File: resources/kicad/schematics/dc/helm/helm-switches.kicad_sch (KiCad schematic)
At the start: 46 parts, among them SW01 CARLING_BLANK, SW02 CARLING_TYPE_28_(ON)-OFF-(ON), SW03 CARLING_TYPE_22_OFF-(ON), SW04 CARLING_TYPE_62_OFF-ON-ON, SW05 CARLING_TYPE_21_OFF-ON, SW06 CARLING_BLANK, SW07 CARLING_BLANK, SW08 CARLING_BLANK, SW09 CARLING_TYPE_21_OFF-ON, SW10 CARLING_TYPE_21_OFF-ON, SW11 CARLING_TYPE_21_OFF-ON, SW12 CARLING_TYPE_21_OFF-ON, SW13 CARLING_TYPE_21_OFF-ON, SW14 CARLING_TYPE_21_OFF-ON, SW15 CARLING_TYPE_21_OFF-ON, SW16 CARLING_TYPE_62_OFF-ON-ON, SW17 CARLING_TYPE_24_ON-ON, SW18 CARLING_TYPE_22_OFF-(ON), SW19 CARLING_TYPE_62_OFF-ON-ON, SW20 CARLING_TYPE_62_OFF-ON-ON, SW21 CARLING_TYPE_62_OFF-ON-ON, SW22 CARLING_TYPE_62_OFF-ON-ON, SW23 CARLING_BLANK, SW24 CARLING_TYPE_62_OFF-ON-ON, SW25 CARLING_TYPE_21_OFF-ON, SW26 CARLING_V_SERIES_ROTARY_TYPE_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, SW27 CARLING_TYPE_62_OFF-ON-ON, SW28 CARLING_TYPE_28_(ON)-OFF-(ON), SW29 CARLING_TYPE_28_(ON)-OFF-(ON), SW30 CARLING_TYPE_28_(ON)-OFF-(ON), SW31 CARLING_TYPE_62_OFF-ON-ON, SW32 CARLING_TYPE_62_OFF-ON-ON, SW33 CARLING_BLANK, SW34 CARLING_BLANK, SW35 CARLING_BLANK, SW36 CARLING_TYPE_62_OFF-ON-ON, SW37 CARLING_TYPE_21_OFF-ON, SW38 CARLING_TYPE_21_OFF-ON, SW39 CARLING_TYPE_26_ON-OFF-ON

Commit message: Updates
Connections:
- net F9.2.1: now also SW37.12 (LED+); no longer SW26.8 (LED+), SW27.10 (LED+), SW27.12 (LED+), SW28.10 (LED+), SW28.2, SW29.10 (LED+), SW29.2, SW30.10 (LED+), SW30.2
- net F9.2.8: no longer SW27.3
- net ENG.IGN renamed IGN.75
- net ENG.IGN.TRL.SBY renamed IGN.75.TRL.SBY
- net IGN.75.TRL.SBY: no longer SW37.12 (LED+)
- net F9.2.1.DKH.OP1: no longer names the net of SW25.12 (LED+), SW25.4
- net F9.2.1.DKH.OP1: now also SW26.8 (LED+), SW27.10 (LED+), SW27.12 (LED+), SW28.10 (LED+), SW28.2, SW29.10 (LED+), SW29.2, SW30.10 (LED+), SW30.2
- new net F9.2.8.THR.ACT: SW27.3
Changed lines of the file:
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@@
 	)
 	(junction
-		(at 67.31 288.29)
-		(diameter 0)
-		(color 0 0 0 0)
-	)
-	(junction
-		(at 67.31 407.67)
-		(diameter 0)
-		(color 0 0 0 0)
-	)
-	(junction
 		(at 334.01 97.79)
 		(diameter 0)
@@
 	)
 	(junction
-		(at 67.31 389.89)
-		(diameter 0)
-		(color 0 0 0 0)
-	)
-	(junction
 		(at 120.65 389.89)
 		(diameter 0)
@@
 	)
 	(junction
+		(at 69.85 397.51)
+		(diameter 0)
+		(color 0 0 0 0)
+	)
+	(junction
 		(at 41.91 397.51)
 		(diameter 0)
@@
 	)
 	(junction
+		(at 95.25 288.29)
+		(diameter 0)
+		(color 0 0 0 0)
+	)
+	(junction
 		(at 227.33 233.68)
 		(diameter 0)
@@
 	)
 	(junction
-		(at 67.31 306.07)
-		(diameter 0)
-		(color 0 0 0 0)
-	)
-	(junction
 		(at 41.91 124.46)
 		(diameter 0)
@@
 	)
 	(junction
+		(at 69.85 389.89)
+		(diameter 0)
+		(color 0 0 0 0)
+	)
+	(junction
 		(at 92.71 226.06)
 		(diameter 0)
@@
 	)
 	(junction
+		(at 69.85 306.07)
+		(diameter 0)
+		(color 0 0 0 0)
+	)
+	(junction
 		(at 41.91 194.31)
 		(diameter 0)
@@
 	)
 	(junction
-		(at 95.25 288.29)
-		(diameter 0)
-		(color 0 0 0 0)
-	)
-	(junction
 		(at 95.25 331.47)
 		(diameter 0)
@@
 	(wire
 		(pts
-			(xy 67.31 389.89) (xy 67.31 397.51)
-		)
-		(stroke
-			(width 0)
-			(type default)
-		)
-	)
-	(wire
-		(pts
 			(xy 171.45 194.31) (xy 173.99 194.31)
 		)
@@
 	(wire
 		(pts
-			(xy 64.77 407.67) (xy 67.31 407.67)
-		)
-		(stroke
-			(width 0)
-			(type default)
-		)
-	)
-	(wire
-		(pts
 			(xy 120.65 31.75) (xy 173.99 31.75)
 		)
@@
 	(wire
 		(pts
-			(xy 69.85 290.83) (xy 69.85 306.07)
+			(xy 69.85 288.29) (xy 69.85 306.07)
 		)
 		(stroke
@@
 	(wire
 		(pts
-			(xy 69.85 306.07) (xy 67.31 306.07)
-		)
-		(stroke
-			(width 0)
-			(type default)
-		)
-	)
-	(wire
-		(pts
 			(xy 173.99 252.73) (xy 173.99 257.81)
 		)
@@
 	(wire
 		(pts
+			(xy 69.85 389.89) (xy 69.85 397.51)
+		)
+		(stroke
+			(width 0)
+			(type default)
+		)
+	)
+	(wire
+		(pts
 			(xy 308.61 257.81) (xy 308.61 252.73)
 		)
@@
 	(wire
 		(pts
-			(xy 31.75 389.89) (xy 67.31 389.89)
+			(xy 31.75 389.89) (xy 69.85 389.89)
 		)
 		(stroke
@@
 	(wire
 		(pts
-			(xy 64.77 410.21) (xy 67.31 410.21)
+			(xy 64.77 410.21) (xy 69.85 410.21)
 		)
 		(stroke
@@
 	(wire
 		(pts
-			(xy 64.77 397.51) (xy 67.31 397.51)
-		)
-		(stroke
-			(width 0)
-			(type default)
-		)
-	)
-	(wire
-		(pts
 			(xy 227.33 128.27) (xy 280.67 128.27)
 		)
@@
 	(wire
 		(pts
-			(xy 71.12 290.83) (xy 69.85 290.83)
-		)
-		(stroke
-			(width 0)
-			(type default)
-		)
-	)
-	(wire
-		(pts
 			(xy 171.45 41.91) (xy 173.99 41.91)
 		)
@@
 	(wire
 		(pts
+			(xy 64.77 402.59) (xy 72.39 402.59)
+		)
+		(stroke
+			(width 0)
+			(type default)
+		)
+	)
+	(wire
+		(pts
 			(xy 95.25 92.71) (xy 95.25 97.79)
 		)
@@
 	(wire
 		(pts
-			(xy 67.31 407.67) (xy 69.85 407.67)
+			(xy 64.77 407.67) (xy 72.39 407.67)
 		)
 		(stroke
@@
 	(wire
 		(pts
-			(xy 67.31 389.89) (xy 120.65 389.89)
-		)
-		(stroke
-			(width 0)
-			(type default)
-		)
-	)
-	(wire
-		(pts
 			(xy 97.79 194.31) (xy 95.25 194.31)
 		)
@@
 	(wire
 		(pts
+			(xy 69.85 397.51) (xy 69.85 410.21)
+		)
+		(stroke
+			(width 0)
+			(type default)
+		)
+	)
+	(wire
+		(pts
 			(xy 120.65 196.85) (xy 120.65 214.63)
 		)
@@
 	(wire
 		(pts
+			(xy 95.25 288.29) (xy 69.85 288.29)
+		)
+		(stroke
+			(width 0)
+			(type default)
+		)
+	)
+	(wire
+		(pts
 			(xy 64.77 351.79) (xy 69.85 351.79)
 		)
@@
 	(wire
 		(pts
-			(xy 64.77 306.07) (xy 67.31 306.07)
+			(xy 64.77 306.07) (xy 69.85 306.07)
 		)
 		(stroke
@@
 	(wire
 		(pts
-			(xy 67.31 410.21) (xy 67.31 407.67)
-		)
-		(stroke
-			(width 0)
-			(type default)
-		)
-	)
-	(wire
-		(pts
 			(xy 201.93 448.31) (xy 201.93 461.01)
 		)
@@
 	(wire
 		(pts
-			(xy 64.77 308.61) (xy 67.31 308.61)
+			(xy 64.77 308.61) (xy 69.85 308.61)
 		)
 		(stroke
@@
 	(wire
 		(pts
-			(xy 67.31 288.29) (xy 95.25 288.29)
-		)
-		(stroke
-			(width 0)
-			(type default)
-		)
-	)
-	(wire
-		(pts
 			(xy 95.25 306.07) (xy 95.25 311.15)
 		)
@@
 	(wire
 		(pts
-			(xy 64.77 402.59) (xy 69.85 402.59)
-		)
-		(stroke
-			(width 0)
-			(type default)
-		)
-	)
-	(wire
-		(pts
 			(xy 97.79 105.41) (xy 95.25 105.41)
 		)
@@
 	(wire
 		(pts
-			(xy 67.31 306.07) (xy 67.31 308.61)
+			(xy 69.85 306.07) (xy 69.85 308.61)
 		)
 		(stroke
@@
 	(wire
 		(pts
+			(xy 64.77 397.51) (xy 69.85 397.51)
+		)
+		(stroke
+			(width 0)
+			(type default)
+		)
+	)
+	(wire
+		(pts
 			(xy 67.31 82.55) (xy 120.65 82.55)
 		)
@@
 	(wire
 		(pts
+			(xy 69.85 389.89) (xy 120.65 389.89)
+		)
+		(stroke
+			(width 0)
+			(type default)
+		)
+	)
+	(wire
+		(pts
 			(xy 331.47 255.27) (xy 336.55 255.27)
 		)
@@
 		)
 	)
-	(global_label "ENG.IGN"
-		(shape input)
-		(at 69.85 402.59 0)
-		(fields_autoplaced yes)
-		(effects
-			(font
-				(size 1.27 1.27)
-			)
-			(justify left)
-		)
-		(property "Intersheetrefs" "${INTERSHEET_REFS}"
-			(at 80.3948 402.59 0)
-			(effects
-				(font
-					(size 1.27 1.27)
-				)
-				(justify left)
-				(hide yes)
-			)
-		)
-	)
 	(global_label "F9.2.1.MST.RAS"
 		(shape output)
@@
 		)
 	)
-	(global_label "F9.2.1.DKH.OP1"
-		(shape output)
-		(at 71.12 290.83 0)
-		(fields_autoplaced yes)
-		(effects
-			(font
-				(size 1.27 1.27)
-			)
-			(justify left)
-		)
-		(property "Intersheetrefs" "${INTERSHEET_REFS}"
-			(at 88.922 290.83 0)
-			(effects
-				(font
-					(size 1.27 1.27)
-				)
-				(justify left)
-				(hide yes)
-			)
-		)
-	)
 	(global_label "F9.2.7"
 		(shape input)
@@
 		)
 	)
-	(global_label "ENG.IGN.TRL.SBY"
+	(global_label "IGN.75.TRL.SBY"
 		(shape output)
-		(at 69.85 407.67 0)
+		(at 72.39 407.67 0)
 		(fields_autoplaced yes)
 		(effects
@@
 		)
 		(property "Intersheetrefs" "${INTERSHEET_REFS}"
-			(at 88.4382 407.67 0)
+			(at 89.6477 407.67 0)
 			(effects
 				(font
@@
 		)
 	)
+	(global_label "IGN.75"
+		(shape input)
+		(at 72.39 402.59 0)
+		(fields_autoplaced yes)
+		(effects
+			(font
+				(size 1.27 1.27)
+				(thickness 0.1588)
+			)
+			(justify left)
+		)
+		(property "Intersheetrefs" "${INTERSHEET_REFS}"
+			(at 81.6043 402.59 0)
+			(effects
+				(font
+					(size 1.27 1.27)
+				)
+				(justify left)
+				(hide yes)
+			)
+		)
+	)
 	(global_label "GND.HPD.PWM.INT"
 		(shape input)
@@
 		)
 	)
-	(global_label "F9.2.8"
+	(global_label "F9.2.8.THR.ACT"
 		(shape input)
 		(at 176.53 303.53 0)
@@
 		)
 		(property "Intersheetrefs" "${INTERSHEET_REFS}"
-			(at 185.4419 303.53 0)
+			(at 193.5458 303.53 0)
 			(effects
 				(font

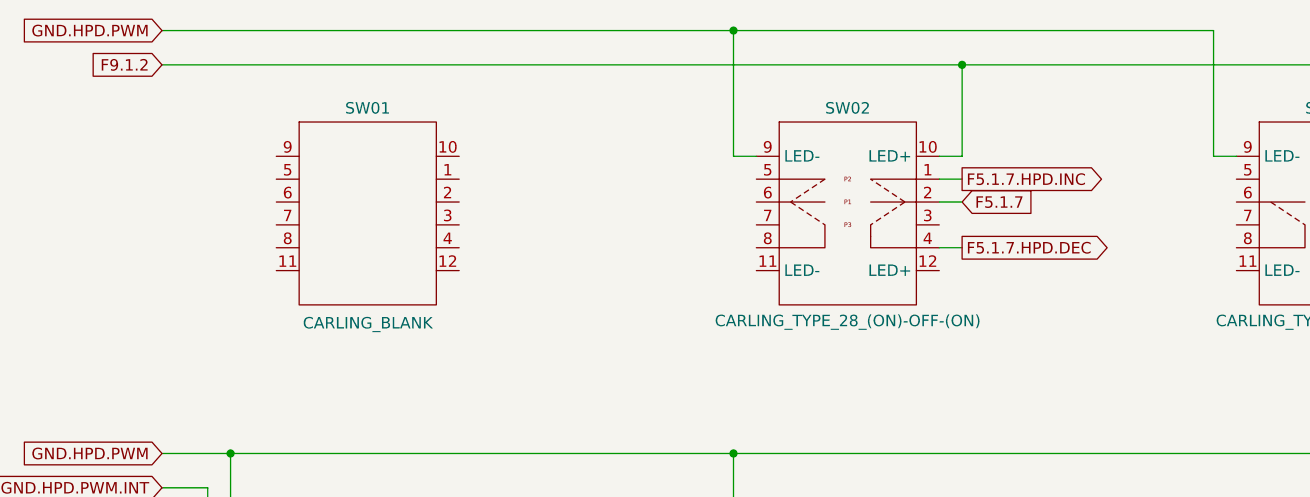
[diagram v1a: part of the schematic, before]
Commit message: Add helm panel lighting on-off feature.
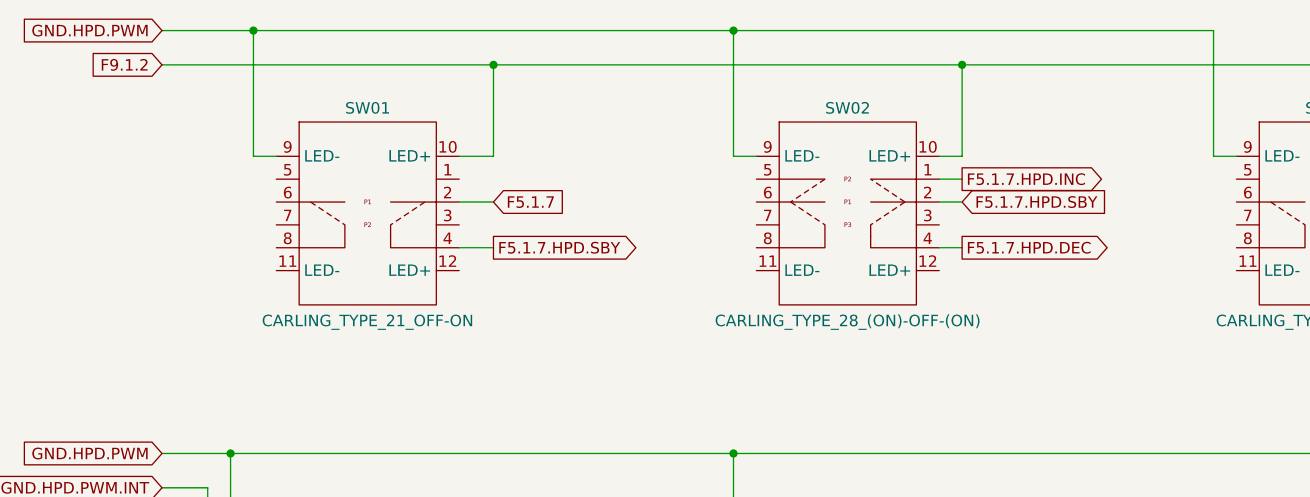
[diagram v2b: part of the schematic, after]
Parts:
- removed SW01: CARLING_BLANK, symbol Switch:Carling_L_Series_Blank
- added SW01: CARLING_TYPE_21_OFF-ON, symbol Switch:Carling_L_Series_Type_21_OFF-ON
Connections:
- net F5.1.7: now also SW01.2; no longer SW02.2
- net F9.1.2: now also SW01.10 (LED+)
- net GND.HPD.PWM: now also SW01.9 (LED-)
- new net F5.1.7.HPD.SBY: SW01.4, SW02.2
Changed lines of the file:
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@@
 	)
 	(junction
+		(at 68.58 31.75)
+		(diameter 0)
+		(color 0 0 0 0)
+	)
+	(junction
 		(at 41.91 194.31)
 		(diameter 0)
@@
 	)
 	(junction
+		(at 41.91 27.94)
+		(diameter 0)
+		(color 0 0 0 0)
+	)
+	(junction
 		(at 92.71 335.28)
 		(diameter 0)
@@
 	(wire
 		(pts
+			(xy 64.77 41.91) (xy 68.58 41.91)
+		)
+		(stroke
+			(width 0)
+			(type default)
+		)
+	)
+	(wire
+		(pts
 			(xy 255.27 143.51) (xy 257.81 143.51)
 		)
@@
 	(wire
 		(pts
+			(xy 64.77 46.99) (xy 68.58 46.99)
+		)
+		(stroke
+			(width 0)
+			(type default)
+		)
+	)
+	(wire
+		(pts
 			(xy 118.11 204.47) (xy 123.19 204.47)
 		)
@@
 	(wire
 		(pts
-			(xy 31.75 27.94) (xy 95.25 27.94)
+			(xy 68.58 31.75) (xy 120.65 31.75)
+		)
+		(stroke
+			(width 0)
+			(type default)
+		)
+	)
+	(wire
+		(pts
+			(xy 31.75 27.94) (xy 41.91 27.94)
 		)
 		(stroke
@@
 	(wire
 		(pts
-			(xy 31.75 31.75) (xy 120.65 31.75)
+			(xy 31.75 31.75) (xy 68.58 31.75)
 		)
 		(stroke
@@
 	(wire
 		(pts
+			(xy 68.58 41.91) (xy 68.58 31.75)
+		)
+		(stroke
+			(width 0)
+			(type default)
+		)
+	)
+	(wire
+		(pts
 			(xy 64.77 351.79) (xy 69.85 351.79)
 		)
@@
 	(wire
 		(pts
+			(xy 41.91 27.94) (xy 41.91 41.91)
+		)
+		(stroke
+			(width 0)
+			(type default)
+		)
+	)
+	(wire
+		(pts
 			(xy 67.31 346.71) (xy 64.77 346.71)
 		)
@@
 	(wire
 		(pts
+			(xy 64.77 52.07) (xy 68.58 52.07)
+		)
+		(stroke
+			(width 0)
+			(type default)
+		)
+	)
+	(wire
+		(pts
 			(xy 67.31 82.55) (xy 67.31 92.71)
 		)
@@
 	(wire
 		(pts
+			(xy 44.45 41.91) (xy 41.91 41.91)
+		)
+		(stroke
+			(width 0)
+			(type default)
+		)
+	)
+	(wire
+		(pts
 			(xy 41.91 199.39) (xy 44.45 199.39)
 		)
@@
 	(wire
 		(pts
+			(xy 41.91 27.94) (xy 95.25 27.94)
+		)
+		(stroke
+			(width 0)
+			(type default)
+		)
+	)
+	(wire
+		(pts
 			(xy 257.81 156.21) (xy 255.27 156.21)
 		)
@@
 		)
 	)
-	(global_label "F5.1.7"
+	(global_label "F5.1.7.HPD.SBY"
 		(shape input)
 		(at 120.65 46.99 0)
@@
 		)
 		(property "Intersheetrefs" "${INTERSHEET_REFS}"
-			(at 129.5619 46.99 0)
+			(at 138.2101 46.99 0)
 			(effects
 				(font
@@
 		)
 	)
+	(global_label "F5.1.7"
+		(shape input)
+		(at 68.58 46.99 0)
+		(fields_autoplaced yes)
+		(effects
+			(font
+				(size 1.27 1.27)
+			)
+			(justify left)
+		)
+		(property "Intersheetrefs" "${INTERSHEET_REFS}"
+			(at 77.4919 46.99 0)
+			(effects
+				(font
+					(size 1.27 1.27)
+				)
+				(justify left)
+				(hide yes)
+			)
+		)
+	)
 	(global_label "F9.1.8.SPD.RAS"
 		(shape output)
@@
 		)
 	)
+	(global_label "F5.1.7.HPD.SBY"
+		(shape output)
+		(at 68.58 52.07 0)
+		(fields_autoplaced yes)
+		(effects
+			(font
+				(size 1.27 1.27)
+			)
+			(justify left)
+		)
+		(property "Intersheetrefs" "${INTERSHEET_REFS}"
+			(at 86.1401 52.07 0)
+			(effects
+				(font
+					(size 1.27 1.27)
+				)
+				(justify left)
+				(hide yes)
+			)
+		)
+	)
 	(global_label "F9.2.1.ANW.LWR"
 		(shape output)
@@
 	(symbol
 		(lib_id "Switch:Carling_L_Series_Blank")
-		(at 54.61 48.26 0)
-		(unit 1)
-		(exclude_from_sim no)
-		(in_bom yes)
-		(on_board yes)
-		(dnp no)
-		(property "Reference" "SW01"
-			(at 54.61 36.576 0)
-			(effects
-				(font
-					(size 1.27 1.27)
-				)
-			)
-		)
-		(property "Value" "CARLING_BLANK"
-			(at 54.61 60.452 0)
-			(effects
-				(font
-					(size 1.27 1.27)
-				)
-			)
-		)
-		(property "Footprint" ""
-			(at 36.322 35.306 0)
-			(effects
-				(font
-					(size 1.27 1.27)
-				)
-				(hide yes)
-			)
-		)
-		(property "Datasheet" ""
-			(at 36.322 35.306 0)
-			(effects
-				(font
-					(size 1.27 1.27)
-				)
-				(hide yes)
-			)
-		)
-		(property "Description" ""
-			(at 36.322 35.306 0)
-			(effects
-				(font
-					(size 1.27 1.27)
-				)
-				(hide yes)
-			)
-		)
-		(pin "8"
-		)
-		(pin "5"
-		)
-		(pin "4"
-		)
-		(pin "7"
-		)
-		(pin "9"
-		)
-		(pin "2"
-		)
-		(pin "10"
-		)
-		(pin "3"
-		)
-		(pin "11"
-		)
-		(pin "1"
-		)
-		(pin "12"
-		)
-		(pin "6"
-		)
-		(instances
-			(project "helm"
-				(path "/a357d5c5-e387-4541-9a53-e66c2daf93af/6a0b4fdf-e9e9-4b14-9b71-1c990e27f3c8"
-					(reference "SW01")
-					(unit 1)
-				)
-			)
-		)
-	)
-	(symbol
-		(lib_id "Switch:Carling_L_Series_Blank")
 		(at 214.63 353.06 0)
 		(unit 1)
@@
 					(unit 1)
 				)
+			)
+		)
+	)
+	(symbol
+		(lib_id "Switch:Carling_L_Series_Type_21_OFF-ON")
+		(at 54.61 48.26 0)
+		(unit 1)
+		(exclude_from_sim no)
+		(in_bom yes)
+		(on_board yes)
+		(dnp no)
+		(property "Reference" "SW01"
+			(at 54.61 36.576 0)
+			(effects
+				(font
+					(size 1.27 1.27)
+				)
+			)
+		)
+		(property "Value" "CARLING_TYPE_21_OFF-ON"
+			(at 54.61 60.198 0)
+			(effects
+				(font
+					(size 1.27 1.27)
+				)
+			)
+		)
+		(property "Footprint" ""
+			(at 36.322 35.306 0)
+			(effects
+				(font
+					(size 1.27 1.27)
+				)
+				(hide yes)
+			)
+		)
+		(property "Datasheet" ""
+			(at 36.322 35.306 0)
+			(effects
+				(font
+					(size 1.27 1.27)
+				)
+				(hide yes)
+			)
+		)
+		(property "Description" ""
+			(at 36.322 35.306 0)
+			(effects
+				(font
+					(size 1.27 1.27)
+				)
+				(hide yes)
+			)
+		)
+		(pin "5"
+		)
+		(pin "4"
+		)
+		(pin "3"
+		)
+		(pin "2"
+		)
+		(pin "12"
+		)
+		(pin "11"
+		)
+		(pin "10"
+		)
+		(pin "1"
+		)
+		(pin "8"
+		)
+		(pin "9"
+		)
+		(pin "6"
+		)
+		(pin "7"
+		)
+		(instances
+			(project ""
+				(path "/a357d5c5-e387-4541-9a53-e66c2daf93af/6a0b4fdf-e9e9-4b14-9b71-1c990e27f3c8"
+					(reference "SW01")
+					(unit 1)
+				)

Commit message: Reformat switch diagram
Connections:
- net F5.1.7.HPD.SBY is gone; now on net F5.1.7.HPD.INC: SW01.4, SW02.2
- net HPD.NEG is gone; now on net GND.HPD.PWM: SW10.6, SW10.9 (LED-), SW11.6, SW11.9 (LED-), SW12.6, SW12.9 (LED-), SW13.6, SW13.9 (LED-), SW14.6, SW14.9 (LED-), SW15.6, SW15.9 (LED-)
- net F9.1.8.SPD.LWR: now also SW39.4
- net F9.1.8.SPD.RAS: now also SW39.1
- net F9.2.1.WNL.OP1: now also SW15.4
- net F9.2.7.WPR.CFG: now also SW16.2; no longer SW16.4
- net F9.2.7.WPR.OP1: now also SW16.4; no longer SW16.2
- net F9.1.8: now reaches SW39.2
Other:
- moved on the sheet: IN1, IN2, IN3, IN4, IN5, IN6, JS01, SW01, SW02, SW03, SW04, SW05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

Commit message: Add wire colors / sizes
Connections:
- net F5.1.7.HPD.INC: no longer SW01.4, SW02.2
- net F9.1.2: now also SW02.2
- new net F5.1.7.HPD.SBY: SW01.4
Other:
- moved on the sheet: IN1, IN2, IN3, IN4, IN5, IN6, JS01, SW01, SW02, SW03, SW04, SW05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
